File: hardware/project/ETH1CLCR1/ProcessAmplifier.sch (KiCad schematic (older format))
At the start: 87 parts, among them Q901 BC847W, Q902 BC847W, Q903 BC847W, U901 TL072, U902 TL072, U903 TL072, U904 TL072, U905 TL071, U906 TL071, U907 AQY212GS, U908 AQY212GS, U909 AQY212GS, U910 AQY212GS, U911 AQY212GS, U912 AQY212GS, U913 AQY212GS, U914 AQY212GS, U915 AQY212GS, U916 AQY212GS, U917 ULN2003A

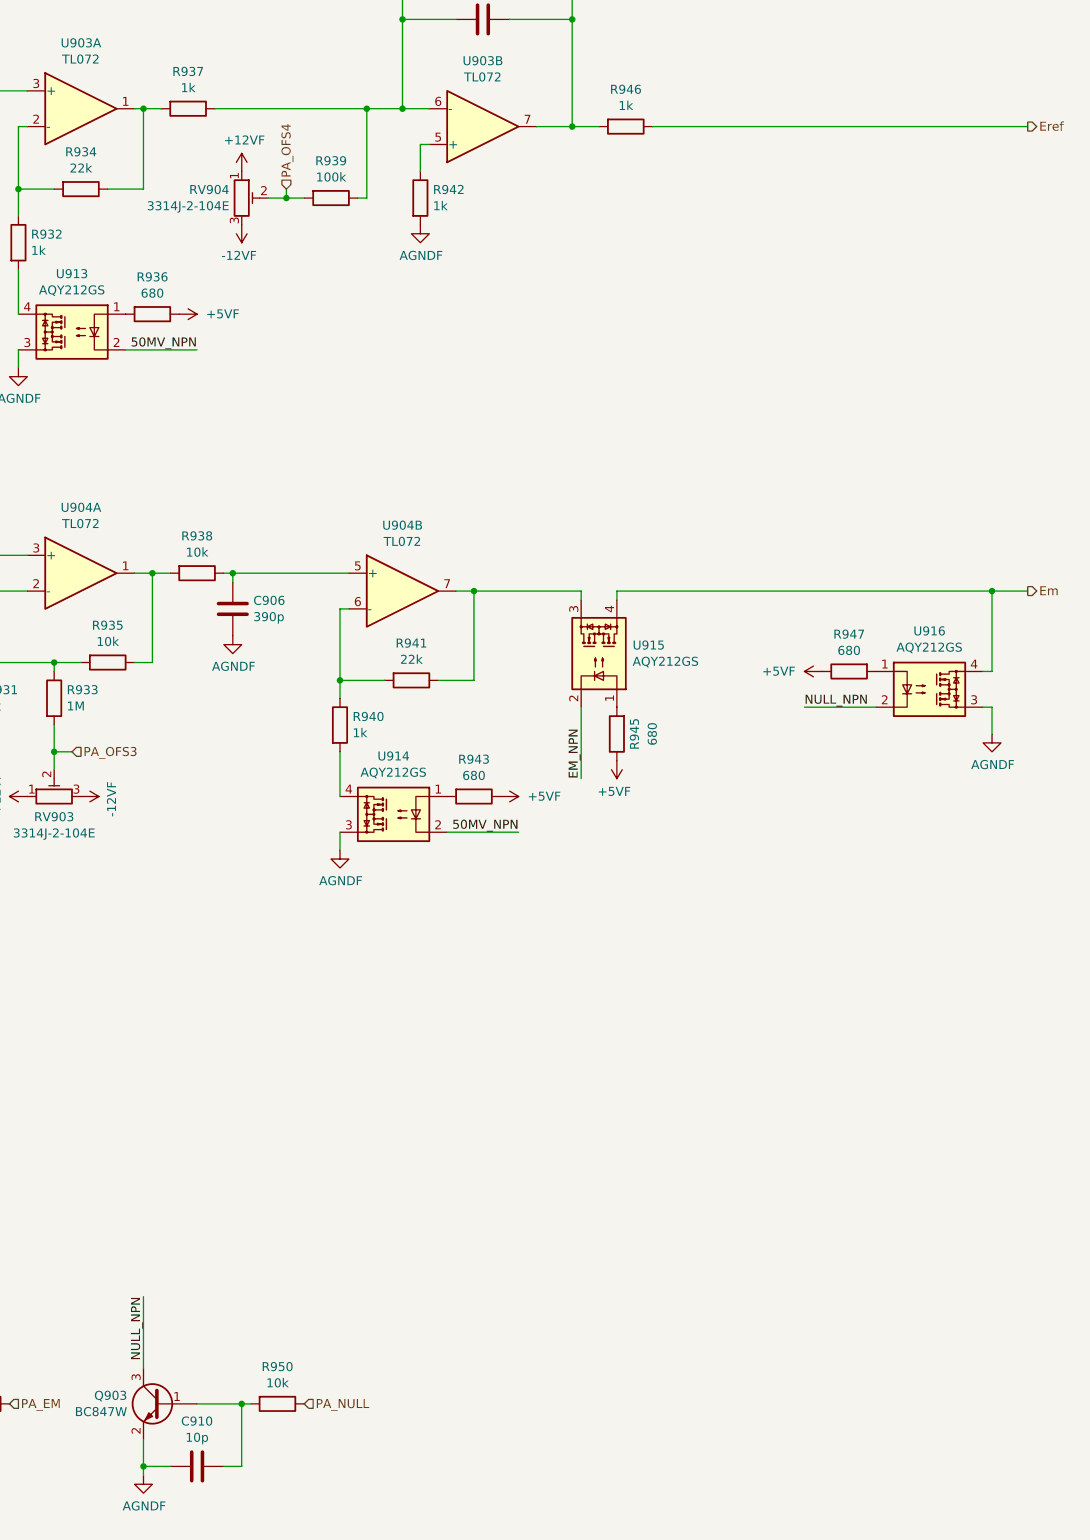
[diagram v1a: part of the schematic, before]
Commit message: Fixed some mistakes in the foorpeints. BOM list ready.
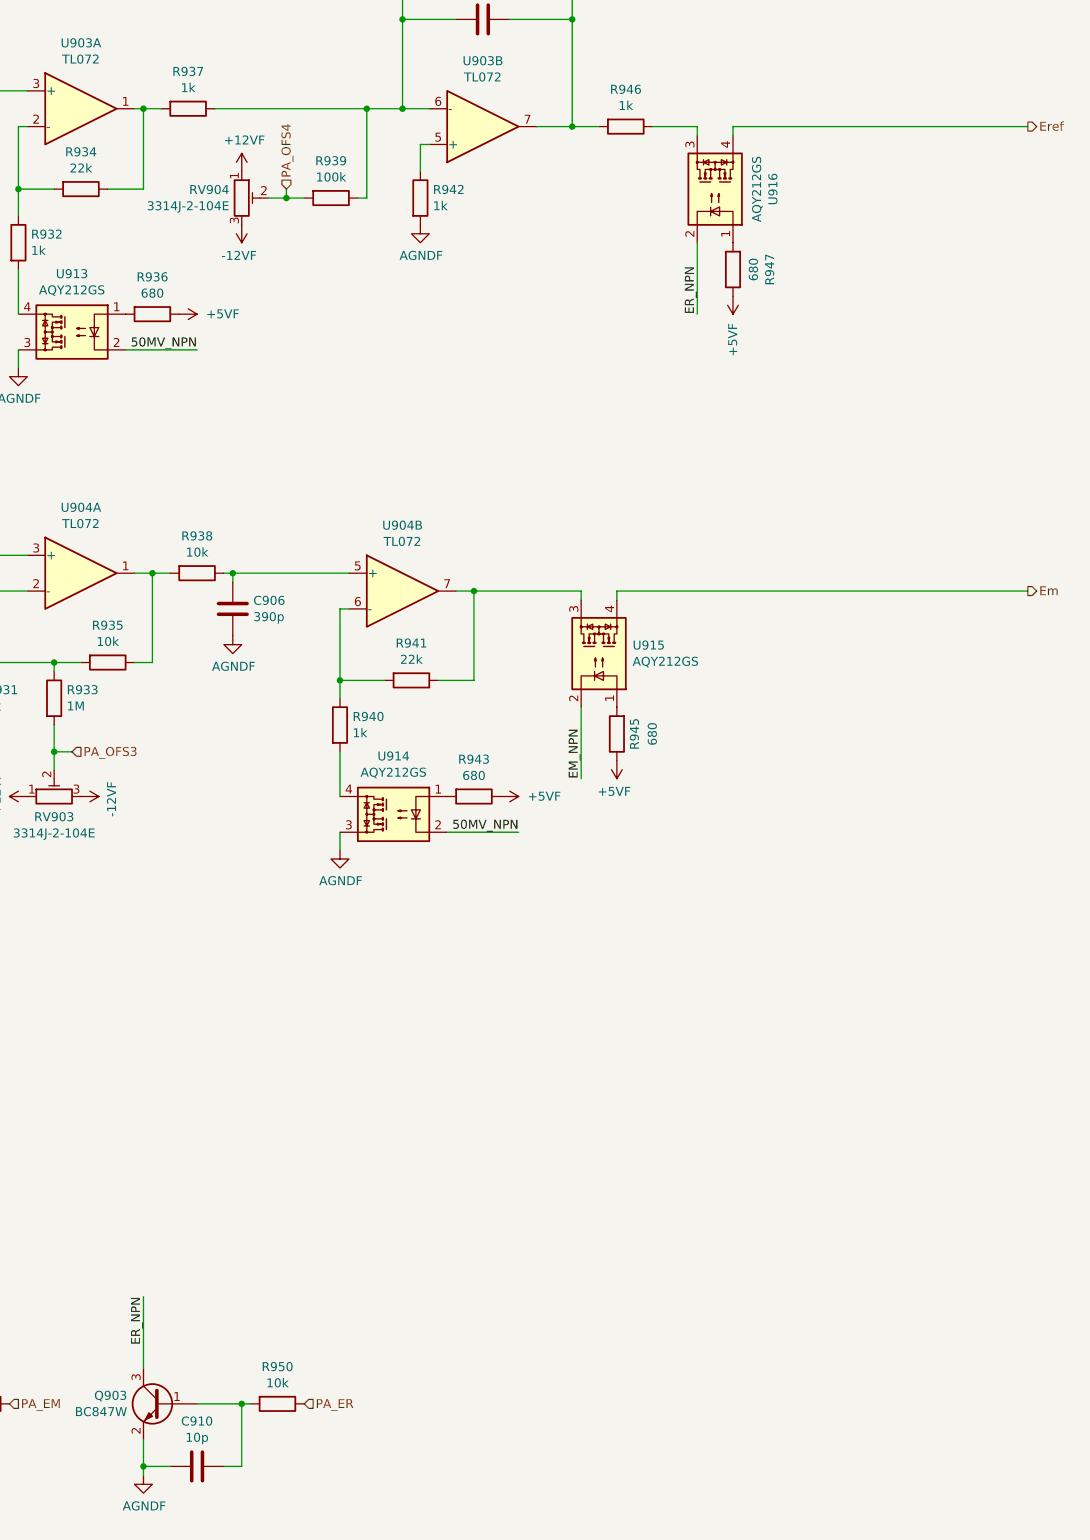
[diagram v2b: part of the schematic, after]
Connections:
- net AGNDF: no longer U916.3
- net Em: no longer U916.4
- net Eref: now also U916.4; no longer R946.1
- net NULL_NPN renamed ER_NPN
- net PA_NULL renamed PA_ER
- new net: R946.1, U916.3
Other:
- moved on the sheet: R947, U916
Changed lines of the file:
@@
 L Device:R R947
 U 1 1 5E340DBC
-P 14250 6050
-F 0 "R947" V 14043 6050 50  0000 C CNN
-F 1 "680" V 14134 6050 50  0000 C CNN
-F 2 "Resistor_SMD:R_0603_1608Metric_Pad1.05x0.95mm_HandSolder" V 14180 6050 50  0001 C CNN
-F 3 "~" H 14250 6050 50  0001 C CNN
-	1    14250 6050
-	0    -1   1    0
-$EndComp
-Wire Wire Line
-	15000 6050 15050 6050
-Wire Wire Line
-	15050 6050 15050 5600
+P 13600 3800
+F 0 "R947" V 13393 3800 50  0000 C CNN
+F 1 "680" V 13484 3800 50  0000 C CNN
+F 2 "Resistor_SMD:R_0603_1608Metric_Pad1.05x0.95mm_HandSolder" V 13530 3800 50  0001 C CNN
+F 3 "~" H 13600 3800 50  0001 C CNN
+	1    13600 3800
+	-1   0    0    1
+$EndComp
 Wire Wire Line
 	12950 5600 12950 5650
-$Comp
-L ETH1CLCR1:AGNDF #PWR0948
-U 1 1 5E35225B
-P 15050 6400
-F 0 "#PWR0948" H 15050 6150 50  0001 C CNN
-F 1 "AGNDF" H 15055 6227 50  0000 C CNN
-F 2 "" H 15050 6400 50  0001 C CNN
-F 3 "" H 15050 6400 50  0001 C CNN
-	1    15050 6400
-	1    0    0    -1
-$EndComp
-Wire Wire Line
-	15050 6400 15050 6250
-Wire Wire Line
-	15050 6250 15000 6250
 Text HLabel 15250 5600 2    50   Output ~ 0
 Em
@@
 	11100 3400 11000 3400
 Wire Wire Line
-	13150 3000 15250 3000
+	13150 3000 13400 3000
 Text HLabel 15250 3000 2    50   Output ~ 0
 Eref
@@
 L ETH1CLCR1:AQY212GS U916
 U 1 1 5E69BE9E
-P 14700 6150
-F 0 "U916" H 14700 6475 50  0000 C CNN
-F 1 "AQY212GS" H 14700 6384 50  0000 C CNN
-F 2 "ETH1CLCR1:AQY212GS" H 14700 6350 50  0001 C CNN
-F 3 "" H 14700 6350 50  0001 C CNN
-	1    14700 6150
-	1    0    0    -1
+P 13500 3350
+F 0 "U916" H 13500 3675 50  0000 C CNN
+F 1 "AQY212GS" H 13500 3584 50  0000 C CNN
+F 2 "ETH1CLCR1:AQY212GS" H 13500 3550 50  0001 C CNN
+F 3 "" H 13500 3550 50  0001 C CNN
+	1    13500 3350
+	0    1    -1   0
 $EndComp
 $Comp
@@
 	-1   0    0    1
 $EndComp
-Connection ~ 15050 5600
-Wire Wire Line
-	15050 5600 15250 5600
-Wire Wire Line
-	12950 5600 15050 5600
 Connection ~ 11550 2900
 Wire Wire Line
@@
 50MV_NPN
 Text Label 10300 9550 3    50   ~ 0
-NULL_NPN
+ER_NPN
 Text HLabel 9550 10150 2    50   Input ~ 0
 PA_EM
 Text HLabel 11200 10150 2    50   Input ~ 0
-PA_NULL
-Wire Wire Line
-	14400 6250 14000 6250
-Text Label 14000 6250 0    50   ~ 0
-NULL_NPN
+PA_ER
+Wire Wire Line
+	13400 3650 13400 4050
+Text Label 13400 4050 1    50   ~ 0
+ER_NPN
 $Comp
 L ETH1CLCR1:+5VF #PWR0953
 U 1 1 604B5CD6
-P 14100 6050
-F 0 "#PWR0953" H 14100 5900 50  0001 C CNN
-F 1 "+5VF" V 14100 6200 50  0000 L CNN
-F 2 "" H 14100 6050 50  0001 C CNN
-F 3 "" H 14100 6050 50  0001 C CNN
-	1    14100 6050
-	0    -1   -1   0
+P 13600 3950
+F 0 "#PWR0953" H 13600 3800 50  0001 C CNN
+F 1 "+5VF" V 13600 4100 50  0000 L CNN
+F 2 "" H 13600 3950 50  0001 C CNN
+F 3 "" H 13600 3950 50  0001 C CNN
+	1    13600 3950
+	1    0    0    1
 $EndComp
 Wire Wire Line
@@
 Wire Wire Line
 	4300 3700 4500 3700
+Wire Wire Line
+	12950 5600 15250 5600
+Wire Wire Line
+	13400 3050 13400 3000
+Wire Wire Line
+	13600 3050 13600 3000
+Wire Wire Line
+	13600 3000 15250 3000
 $EndSCHEMATC

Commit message: PCB layout
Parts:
- added C911, C912, C913, C914, C915, C916, C917, C918, C919, C920, C921, C922, C923: 100n, Capacitor_SMD:C_0603_1608Metric_Pad1.05x0.95mm_HandSolder, symbol Device:C
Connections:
- net +12VF: now also C911.1, C912.1, C913.1, C914.1, C915.1, C916.1
- net +5VF: now also C923.1
- net -12VF: now also C917.1, C918.1, C919.1, C920.1, C921.1, C922.1
- net AGNDF: now also C911.2, C912.2, C913.2, C914.2, C915.2, C916.2, C917.2, C918.2, C919.2, C920.2, C921.2, C922.2, C923.2
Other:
- moved on the sheet: C908, C909, C910, Q901, Q902, Q903, R948, R949, R950, U917

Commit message: PCB layout
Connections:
- net MOS1: now also U917.15 (O2); no longer U917.16 (O1)
- net MOS2: now also U917.16 (O1); no longer U917.15 (O2)
- net MOS3: now also U917.13 (O4); no longer U917.14 (O3)
- net MOS4: now also U917.14 (O3); no longer U917.13 (O4)
- net MOS5: now also U917.11 (O6); no longer U917.12 (O5)
- net MOS6: now also U917.12 (O5); no longer U917.11 (O6)
- net PA_MOS1: now also U917.2 (I2); no longer U917.1 (I1)
- net PA_MOS2: now also U917.1 (I1); no longer U917.2 (I2)
- net PA_MOS3: now also U917.4 (I4); no longer U917.3 (I3)
- net PA_MOS4: now also U917.3 (I3); no longer U917.4 (I4)
- net PA_MOS5: now also U917.6 (I6); no longer U917.5 (I5)
- net PA_MOS6: now also U917.5 (I5); no longer U917.6 (I6)
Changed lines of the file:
@@
 	1    0    0    -1
 $EndComp
+Text HLabel 14650 8900 0    50   Input ~ 0
+PA_MOS1
 Text HLabel 14650 8800 0    50   Input ~ 0
-PA_MOS1
-Text HLabel 14650 8900 0    50   Input ~ 0
 PA_MOS2
+Text HLabel 14650 9100 0    50   Input ~ 0
+PA_MOS3
 Text HLabel 14650 9000 0    50   Input ~ 0
-PA_MOS3
-Text HLabel 14650 9100 0    50   Input ~ 0
 PA_MOS4
+Text HLabel 14650 9300 0    50   Input ~ 0
+PA_MOS5
 Text HLabel 14650 9200 0    50   Input ~ 0
-PA_MOS5
-Text HLabel 14650 9300 0    50   Input ~ 0
 PA_MOS6
 $Comp
@@
 $EndComp
 Wire Wire Line
+	15450 8900 15800 8900
+Wire Wire Line
 	15450 8800 15800 8800
 Wire Wire Line
-	15450 8900 15800 8900
+	15450 9100 15800 9100
 Wire Wire Line
 	15450 9000 15800 9000
 Wire Wire Line
-	15450 9100 15800 9100
+	15450 9300 15800 9300
 Wire Wire Line
 	15450 9200 15800 9200
-Wire Wire Line
-	15450 9300 15800 9300
 NoConn ~ 14650 9400
 NoConn ~ 15450 9400
+Text Label 15800 8900 2    50   ~ 0
+MOS1
 Text Label 15800 8800 2    50   ~ 0
-MOS1
-Text Label 15800 8900 2    50   ~ 0
 MOS2
+Text Label 15800 9100 2    50   ~ 0
+MOS3
 Text Label 15800 9000 2    50   ~ 0
-MOS3
-Text Label 15800 9100 2    50   ~ 0
 MOS4
+Text Label 15800 9300 2    50   ~ 0
+MOS5
 Text Label 15800 9200 2    50   ~ 0
-MOS5
-Text Label 15800 9300 2    50   ~ 0
 MOS6
 Text Label 7700 2800 0    50   ~ 0

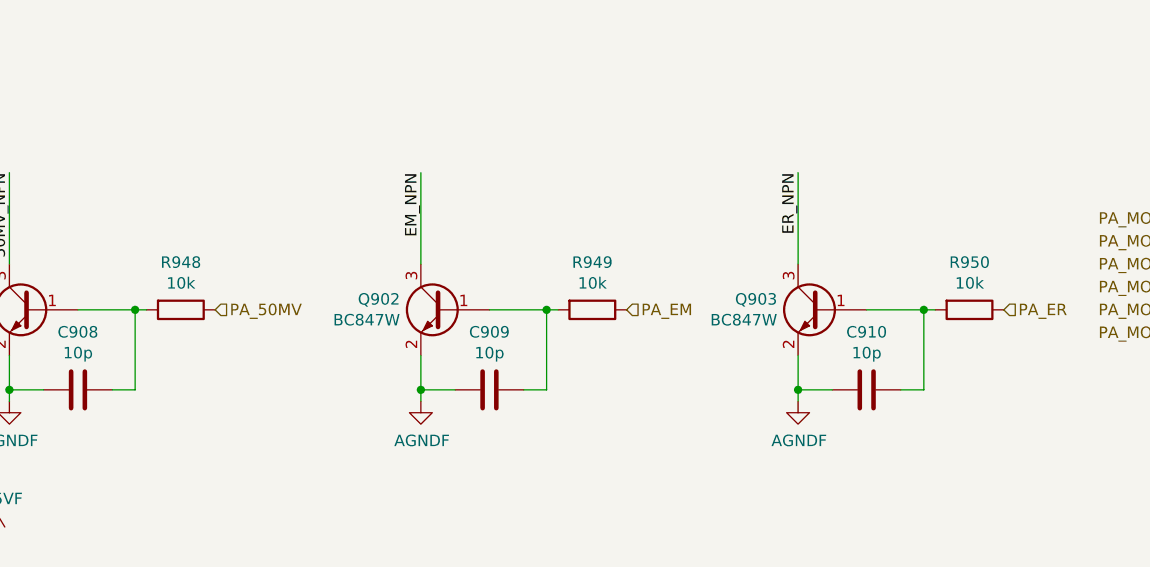
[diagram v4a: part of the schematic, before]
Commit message: Range BC847 base serial resistors value from 10k to 1k.
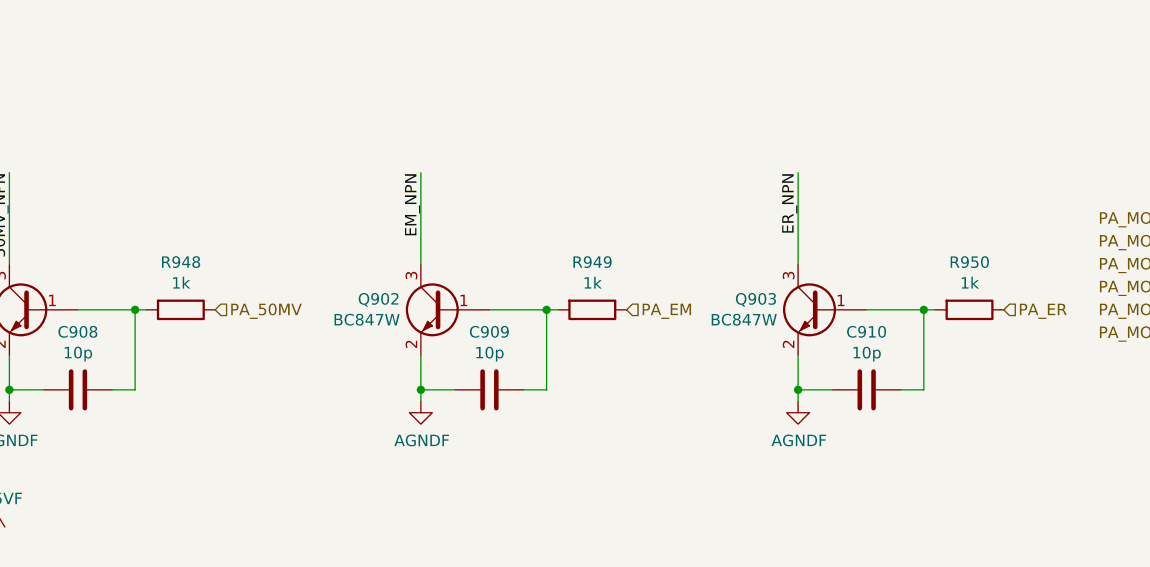
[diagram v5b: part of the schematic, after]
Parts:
- R948, R949, R950: value 10k -> 1k
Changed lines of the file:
@@
 AR Path="/5EB3D8D6/6030F2C1" Ref="R948"  Part="1"
 F 0 "R948" V 10043 9200 50  0000 C CNN
-F 1 "10k" V 10134 9200 50  0000 C CNN
+F 1 "1k" V 10134 9200 50  0000 C CNN
 F 2 "Resistor_SMD:R_0603_1608Metric_Pad1.05x0.95mm_HandSolder" V 10180 9200 50  0001 C CNN
 F 3 "~" H 10250 9200 50  0001 C CNN
@@
 AR Path="/5EB3D8D6/6030F2E3" Ref="R949"  Part="1"
 F 0 "R949" V 11843 9200 50  0000 C CNN
-F 1 "10k" V 11934 9200 50  0000 C CNN
+F 1 "1k" V 11934 9200 50  0000 C CNN
 F 2 "Resistor_SMD:R_0603_1608Metric_Pad1.05x0.95mm_HandSolder" V 11980 9200 50  0001 C CNN
 F 3 "~" H 12050 9200 50  0001 C CNN
@@
 AR Path="/5EB3D8D6/6030F305" Ref="R950"  Part="1"
 F 0 "R950" V 13493 9200 50  0000 C CNN
-F 1 "10k" V 13584 9200 50  0000 C CNN
+F 1 "1k" V 13584 9200 50  0000 C CNN
 F 2 "Resistor_SMD:R_0603_1608Metric_Pad1.05x0.95mm_HandSolder" V 13630 9200 50  0001 C CNN
 F 3 "~" H 13700 9200 50  0001 C CNN

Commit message: Changed BC847W base resistor from 1k to 10k.
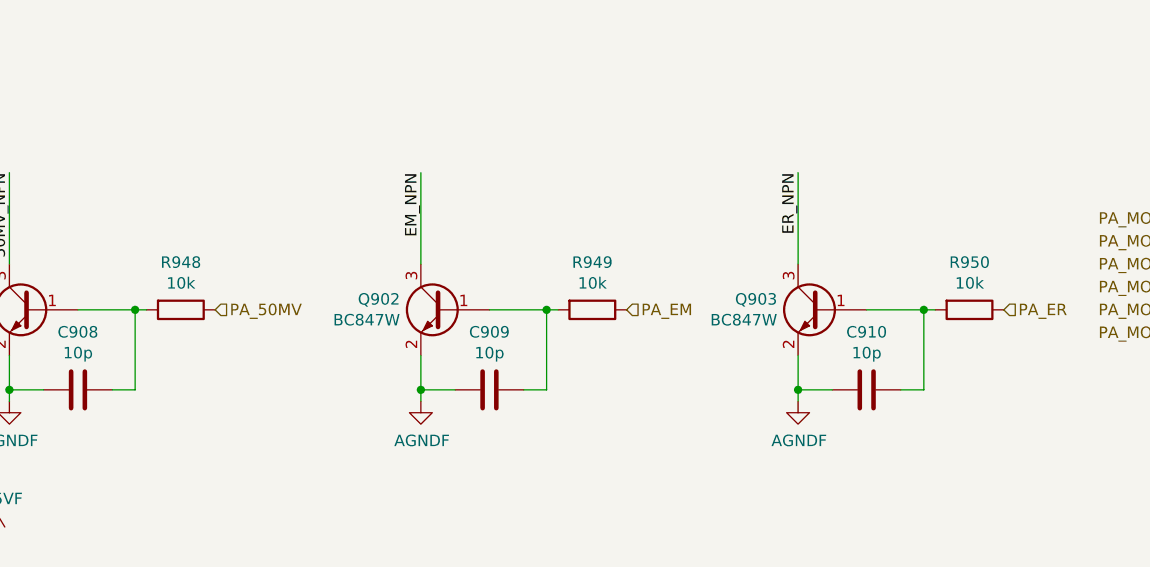
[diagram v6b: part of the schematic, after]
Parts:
- R948, R949, R950: value 1k -> 10k
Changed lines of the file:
@@
 AR Path="/5EB3D8D6/6030F2C1" Ref="R948"  Part="1"
 F 0 "R948" V 10043 9200 50  0000 C CNN
-F 1 "1k" V 10134 9200 50  0000 C CNN
+F 1 "10k" V 10134 9200 50  0000 C CNN
 F 2 "Resistor_SMD:R_0603_1608Metric_Pad1.05x0.95mm_HandSolder" V 10180 9200 50  0001 C CNN
 F 3 "~" H 10250 9200 50  0001 C CNN
@@
 AR Path="/5EB3D8D6/6030F2E3" Ref="R949"  Part="1"
 F 0 "R949" V 11843 9200 50  0000 C CNN
-F 1 "1k" V 11934 9200 50  0000 C CNN
+F 1 "10k" V 11934 9200 50  0000 C CNN
 F 2 "Resistor_SMD:R_0603_1608Metric_Pad1.05x0.95mm_HandSolder" V 11980 9200 50  0001 C CNN
 F 3 "~" H 12050 9200 50  0001 C CNN
@@
 AR Path="/5EB3D8D6/6030F305" Ref="R950"  Part="1"
 F 0 "R950" V 13493 9200 50  0000 C CNN
-F 1 "1k" V 13584 9200 50  0000 C CNN
+F 1 "10k" V 13584 9200 50  0000 C CNN
 F 2 "Resistor_SMD:R_0603_1608Metric_Pad1.05x0.95mm_HandSolder" V 13630 9200 50  0001 C CNN
 F 3 "~" H 13700 9200 50  0001 C CNN
